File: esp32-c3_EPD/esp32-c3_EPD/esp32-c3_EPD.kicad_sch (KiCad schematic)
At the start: 2 parts, among them U1 ESP32-C3 SuperMini

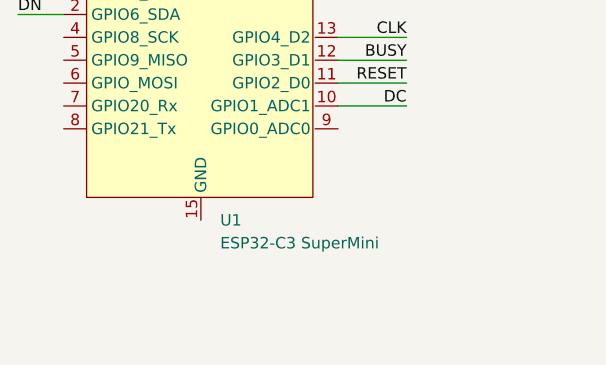
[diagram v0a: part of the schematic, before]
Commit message: ESP32-C3 ePaper
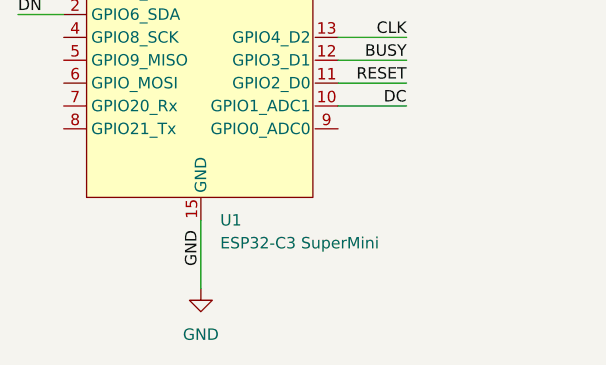
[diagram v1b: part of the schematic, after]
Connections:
- net GND: now also U1.15 (GND)
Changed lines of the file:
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@@
+	(wire
+		(pts
+			(xy 120.65 116.84) (xy 120.65 124.46)
+		)
+		(stroke
+			(width 0)
+			(type default)
+		)
+	)
 	(wire
 		(pts
@@
 	(label "DC"
 		(at 195.58 95.25 90)
+		(effects
+			(font
+				(size 1.27 1.27)
+			)
+			(justify left bottom)
+		)
+	)
+	(label "GND"
+		(at 120.65 121.92 90)
 		(effects
 			(font
@@
 					(unit 1)
 				)
+			)
+		)
+	)
+	(symbol
+		(lib_id "power:GND")
+		(at 120.65 124.46 0)
+		(unit 1)
+		(exclude_from_sim no)
+		(in_bom yes)
+		(on_board yes)
+		(dnp no)
+		(fields_autoplaced yes)
+		(property "Reference" "#PWR01"
+			(at 120.65 130.81 0)
+			(effects
+				(font
+					(size 1.27 1.27)
+				)
+				(hide yes)
+			)
+		)
+		(property "Value" "GND"
+			(at 120.65 129.54 0)
+			(effects
+				(font
+					(size 1.27 1.27)
+				)
+			)
+		)
+		(property "Footprint" ""
+			(at 120.65 124.46 0)
+			(effects
+				(font
+					(size 1.27 1.27)
+				)
+				(hide yes)
+			)
+		)
+		(property "Datasheet" ""
+			(at 120.65 124.46 0)
+			(effects
+				(font
+					(size 1.27 1.27)
+				)
+				(hide yes)
+			)
+		)
+		(property "Description" "Power symbol creates a global label with name \"GND\" , ground"
+			(at 120.65 124.46 0)
+			(effects
+				(font
+					(size 1.27 1.27)
+				)
+				(hide yes)
+			)
+		)
+		(pin "1"
+		)
+		(instances
+			(project ""
+				(path "/344294fb-c5f2-408b-9dcd-2ef32aaa9090"
+					(reference "#PWR01")
+					(unit 1)
+				)

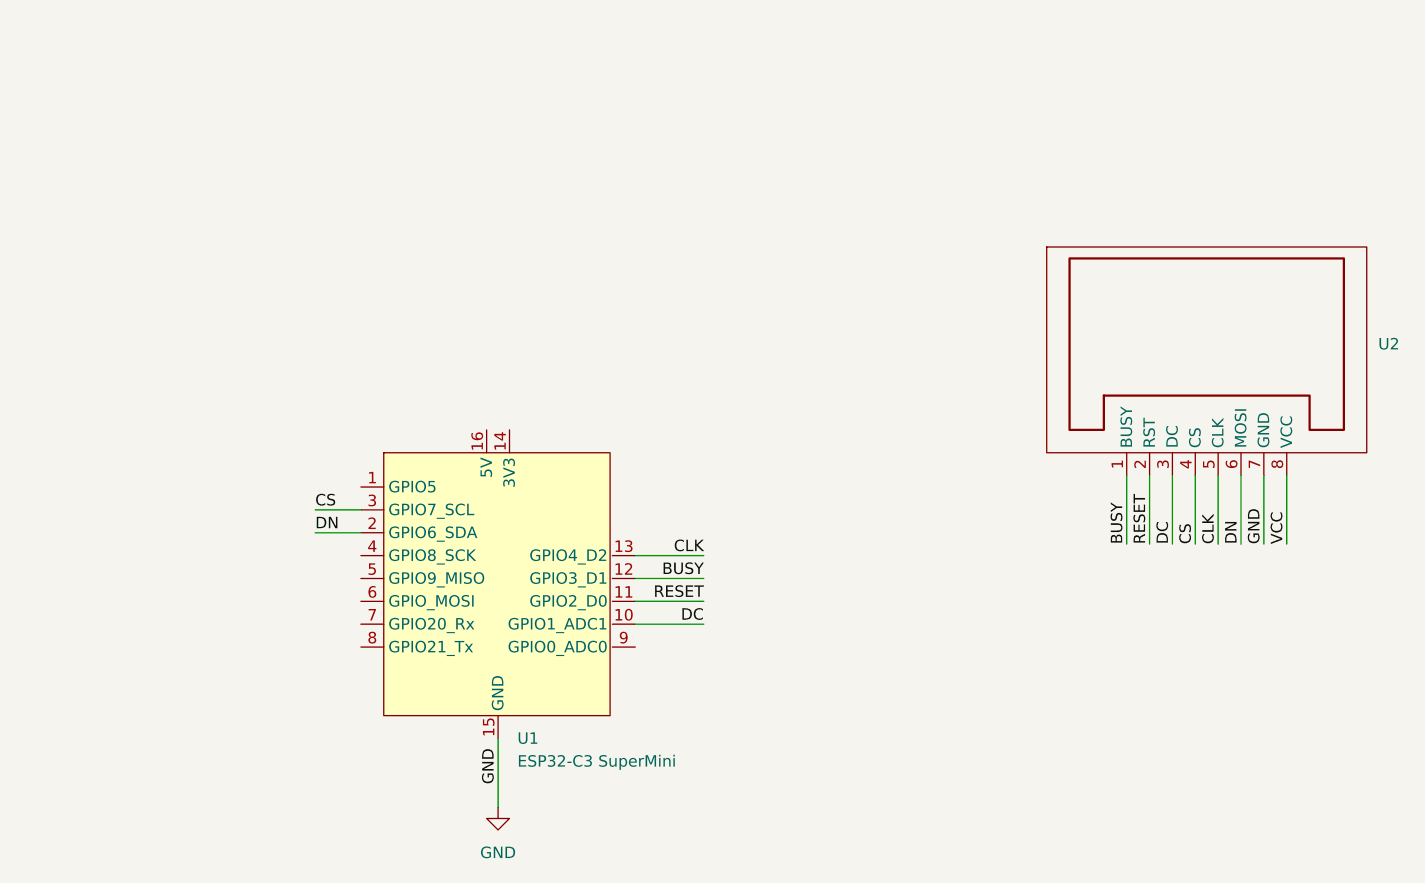
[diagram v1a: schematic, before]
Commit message: ESP32-C3 ePaper
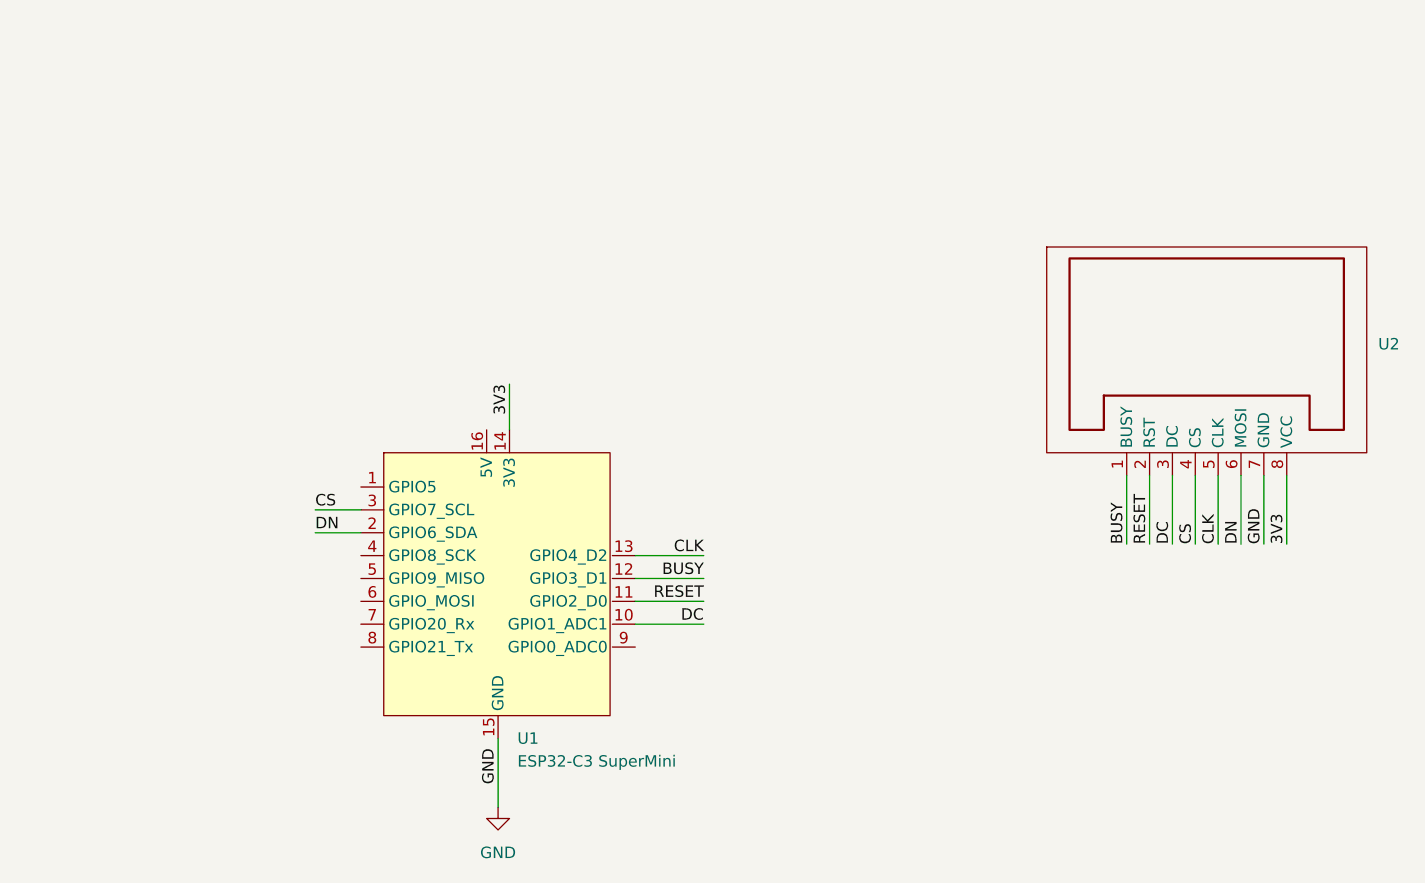
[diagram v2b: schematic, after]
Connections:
- net VCC is gone; now on net 3V3: U2.8 (VCC)
- net 3V3: now reaches U1.14 (3V3)
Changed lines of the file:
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@@
+	(wire
+		(pts
+			(xy 121.92 77.47) (xy 121.92 82.55)
+		)
+		(stroke
+			(width 0)
+			(type default)
+		)
+	)
 	(wire
 		(pts
@@
 		)
 	)
-	(label "VCC"
+	(label "3V3"
+		(at 121.92 77.47 270)
+		(effects
+			(font
+				(size 1.27 1.27)
+			)
+			(justify right bottom)
+		)
+	)
+	(label "3V3"
 		(at 208.28 95.25 90)
 		(effects

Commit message: .
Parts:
- removed U2: ~, symbol Alexander Symbols Library:ePaper
- added J1: e-Paper, Alexander Footprints Library:Conn_ePaper, symbol Alexander Symbols Library:Conn_ePaper_01x08
- U1: footprint Alexander Footprint Library:ESP32-C3_SuperMini -> Alexander Footprints Library:ESP32-C3_SuperMini
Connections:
- net 3V3: now also J1.Vcc
- net BUSY: now also J1.BUSY
- net CLK: now also J1.CLK
- net CS: now also J1.DC
- net DC: now also J1.RST
- net DN: now also J1.DIN
- net GND: now also J1.GND
- net RESET: now also J1.CS
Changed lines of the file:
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@@
 	(wire
 		(pts
-			(xy 198.12 87.63) (xy 198.12 95.25)
+			(xy 144.78 53.34) (xy 158.75 53.34)
 		)
 		(stroke
@@
 	(wire
 		(pts
-			(xy 190.5 87.63) (xy 190.5 95.25)
-		)
-		(stroke
-			(width 0)
-			(type default)
-		)
-	)
-	(wire
-		(pts
-			(xy 208.28 87.63) (xy 208.28 95.25)
+			(xy 144.78 45.72) (xy 158.75 45.72)
+		)
+		(stroke
+			(width 0)
+			(type default)
+		)
+	)
+	(wire
+		(pts
+			(xy 144.78 43.18) (xy 158.75 43.18)
 		)
 		(stroke
@@
 	(wire
 		(pts
-			(xy 193.04 87.63) (xy 193.04 95.25)
-		)
-		(stroke
-			(width 0)
-			(type default)
-		)
-	)
-	(wire
-		(pts
-			(xy 203.2 87.63) (xy 203.2 95.25)
-		)
-		(stroke
-			(width 0)
-			(type default)
-		)
-	)
-	(wire
-		(pts
-			(xy 195.58 87.63) (xy 195.58 95.25)
-		)
-		(stroke
-			(width 0)
-			(type default)
-		)
-	)
-	(wire
-		(pts
-			(xy 200.66 87.63) (xy 200.66 95.25)
-		)
-		(stroke
-			(width 0)
-			(type default)
-		)
-	)
-	(wire
-		(pts
-			(xy 205.74 87.63) (xy 205.74 95.25)
+			(xy 144.78 48.26) (xy 158.75 48.26)
+		)
+		(stroke
+			(width 0)
+			(type default)
+		)
+	)
+	(wire
+		(pts
+			(xy 144.78 58.42) (xy 158.75 58.42)
+		)
+		(stroke
+			(width 0)
+			(type default)
+		)
+	)
+	(wire
+		(pts
+			(xy 144.78 50.8) (xy 158.75 50.8)
+		)
+		(stroke
+			(width 0)
+			(type default)
+		)
+	)
+	(wire
+		(pts
+			(xy 144.78 55.88) (xy 158.75 55.88)
+		)
+		(stroke
+			(width 0)
+			(type default)
+		)
+	)
+	(wire
+		(pts
+			(xy 144.78 60.96) (xy 158.75 60.96)
 		)
 		(stroke
@@
 	)
 	(label "GND"
-		(at 205.74 95.25 90)
+		(at 144.78 60.96 0)
 		(effects
 			(font
@@
 	)
 	(label "3V3"
-		(at 208.28 95.25 90)
+		(at 144.78 43.18 0)
 		(effects
 			(font
@@
 	)
 	(label "RESET"
-		(at 193.04 95.25 90)
+		(at 144.78 48.26 0)
 		(effects
 			(font
@@
 	)
 	(label "DN"
-		(at 203.2 95.25 90)
+		(at 144.78 58.42 0)
 		(effects
 			(font
@@
 	)
 	(label "BUSY"
-		(at 190.5 95.25 90)
+		(at 144.78 45.72 0)
 		(effects
 			(font
@@
 	)
 	(label "CS"
-		(at 198.12 95.25 90)
+		(at 144.78 53.34 0)
 		(effects
 			(font
@@
 	)
 	(label "DC"
-		(at 195.58 95.25 90)
+		(at 144.78 50.8 0)
 		(effects
 			(font
@@
 	)
 	(label "CLK"
-		(at 200.66 95.25 90)
+		(at 144.78 55.88 0)
 		(effects
 			(font
@@
 			)
 		)
-		(property "Footprint" "Alexander Footprint Library:ESP32-C3_SuperMini"
+		(property "Footprint" "Alexander Footprints Library:ESP32-C3_SuperMini"
 			(at 94.234 79.502 0)
 			(effects
@@
 				(path "/344294fb-c5f2-408b-9dcd-2ef32aaa9090"
 					(reference "U1")
-					(unit 1)
-				)
-			)
-		)
-	)
-	(symbol
-		(lib_id "Alexander Symbols Library:ePaper")
-		(at 199.39 59.69 0)
-		(unit 1)
-		(exclude_from_sim no)
-		(in_bom yes)
-		(on_board yes)
-		(dnp no)
-		(fields_autoplaced yes)
-		(property "Reference" "U2"
-			(at 218.44 73.0249 0)
-			(effects
-				(font
-					(size 1.27 1.27)
-				)
-				(justify left)
-			)
-		)
-		(property "Value" "~"
-			(at 218.44 74.93 0)
-			(effects
-				(font
-					(size 1.27 1.27)
-				)
-				(justify left)
-			)
-		)
-		(property "Footprint" ""
-			(at 199.39 59.69 0)
-			(effects
-				(font
-					(size 1.27 1.27)
-				)
-				(hide yes)
-			)
-		)
-		(property "Datasheet" ""
-			(at 199.39 59.69 0)
-			(effects
-				(font
-					(size 1.27 1.27)
-				)
-				(hide yes)
-			)
-		)
-		(property "Description" ""
-			(at 199.39 59.69 0)
-			(effects
-				(font
-					(size 1.27 1.27)
-				)
-				(hide yes)
-			)
-		)
-		(pin "1"
-		)
-		(pin "4"
-		)
-		(pin "3"
-		)
-		(pin "5"
-		)
-		(pin "7"
-		)
-		(pin "6"
-		)
-		(pin "8"
-		)
-		(pin "2"
-		)
-		(instances
-			(project ""
-				(path "/344294fb-c5f2-408b-9dcd-2ef32aaa9090"
-					(reference "U2")
 					(unit 1)
 				)
@@
 					(unit 1)
 				)
+			)
+		)
+	)
+	(symbol
+		(lib_id "Alexander Symbols Library:Conn_ePaper_01x08")
+		(at 163.83 50.8 0)
+		(mirror y)
+		(unit 1)
+		(exclude_from_sim no)
+		(in_bom yes)
+		(on_board yes)
+		(dnp no)
+		(property "Reference" "J1"
+			(at 163.195 38.1 0)
+			(effects
+				(font
+					(size 1.27 1.27)
+				)
+			)
+		)
+		(property "Value" "e-Paper"
+			(at 163.195 40.64 0)
+			(effects
+				(font
+					(size 1.27 1.27)
+				)
+			)
+		)
+		(property "Footprint" "Alexander Footprints Library:Conn_ePaper"
+			(at 163.83 55.88 0)
+			(effects
+				(font
+					(size 1.27 1.27)
+				)
+				(hide yes)
+			)
+		)
+		(property "Datasheet" "~"
+			(at 165.1 52.07 0)
+			(effects
+				(font
+					(size 1.27 1.27)
+				)
+				(hide yes)
+			)
+		)
+		(property "Description" "Generic connector, single row, 01x08, script generated"
+			(at 163.83 50.8 0)
+			(effects
+				(font
+					(size 1.27 1.27)
+				)
+				(hide yes)
+			)
+		)
+		(pin "GND"
+		)
+		(pin "RST"
+		)
+		(pin "CLK"
+		)
+		(pin "CS"
+		)
+		(pin "DC"
+		)
+		(pin "BUSY"
+		)
+		(pin "Vcc"
+		)
+		(pin "DIN"
+		)
+		(instances
+			(project ""
+				(path "/344294fb-c5f2-408b-9dcd-2ef32aaa9090"
+					(reference "J1")
+					(unit 1)
+				)

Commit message: .
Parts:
- added U2: ESP32-C3 WROOM, symbol Alexander Symbols Library 1:ESP32-C3_Mini
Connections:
- net 3V3: now also U2.1 (3V3)
- net BUSY: now also U2.15 (GPIO3)
- net CLK: now also U2.3 (GPIO4)
- net CS: now also U2.6 (GPIO7)
- net DN: now also U2.5 (GPIO6)
- net GND: now also U2.9 (GND)
- net RESET: now also U2.16 (GPIO2)
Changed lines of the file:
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@@
+	(wire
+		(pts
+			(xy 67.31 57.15) (xy 73.66 57.15)
+		)
+		(stroke
+			(width 0)
+			(type default)
+		)
+	)
+	(wire
+		(pts
+			(xy 105.41 54.61) (xy 113.03 54.61)
+		)
+		(stroke
+			(width 0)
+			(type default)
+		)
+	)
+	(wire
+		(pts
+			(xy 67.31 59.69) (xy 73.66 59.69)
+		)
+		(stroke
+			(width 0)
+			(type default)
+		)
+	)
+	(wire
+		(pts
+			(xy 67.31 52.07) (xy 73.66 52.07)
+		)
+		(stroke
+			(width 0)
+			(type default)
+		)
+	)
 	(wire
 		(pts
@@
 	(wire
 		(pts
+			(xy 67.31 46.99) (xy 73.66 46.99)
+		)
+		(stroke
+			(width 0)
+			(type default)
+		)
+	)
+	(wire
+		(pts
 			(xy 135.89 99.06) (xy 143.51 99.06)
 		)
@@
 	(wire
 		(pts
+			(xy 105.41 52.07) (xy 113.03 52.07)
+		)
+		(stroke
+			(width 0)
+			(type default)
+		)
+	)
+	(wire
+		(pts
 			(xy 121.92 77.47) (xy 121.92 82.55)
+		)
+		(stroke
+			(width 0)
+			(type default)
+		)
+	)
+	(wire
+		(pts
+			(xy 67.31 67.31) (xy 73.66 67.31)
 		)
 		(stroke
@@
 	)
 	(label "3V3"
+		(at 67.31 46.99 0)
+		(effects
+			(font
+				(size 1.27 1.27)
+			)
+			(justify left bottom)
+		)
+	)
+	(label "DN"
+		(at 67.31 57.15 0)
+		(effects
+			(font
+				(size 1.27 1.27)
+			)
+			(justify left bottom)
+		)
+	)
+	(label "3V3"
 		(at 121.92 77.47 270)
 		(effects
@@
 		)
 	)
+	(label "CLK"
+		(at 67.31 52.07 0)
+		(effects
+			(font
+				(size 1.27 1.27)
+			)
+			(justify left bottom)
+		)
+	)
 	(label "CS"
 		(at 100.33 91.44 0)
@@
 		)
 	)
+	(label "CS"
+		(at 67.31 59.69 0)
+		(effects
+			(font
+				(size 1.27 1.27)
+			)
+			(justify left bottom)
+		)
+	)
+	(label "RESET"
+		(at 113.03 52.07 180)
+		(effects
+			(font
+				(size 1.27 1.27)
+			)
+			(justify right bottom)
+		)
+	)
 	(label "DC"
 		(at 143.51 104.14 180)
@@
 		)
 	)
+	(label "BUSY"
+		(at 113.03 54.61 180)
+		(effects
+			(font
+				(size 1.27 1.27)
+			)
+			(justify right bottom)
+		)
+	)
 	(label "DN"
 		(at 144.78 58.42 0)
@@
 	(label "GND"
 		(at 120.65 121.92 90)
+		(effects
+			(font
+				(size 1.27 1.27)
+			)
+			(justify left bottom)
+		)
+	)
+	(label "GND"
+		(at 67.31 67.31 0)
 		(effects
 			(font
@@
 					(unit 1)
 				)
+			)
+		)
+	)
+	(symbol
+		(lib_id "Alexander Symbols Library 1:ESP32-C3_Mini")
+		(at 88.9 41.91 0)
+		(unit 1)
+		(exclude_from_sim no)
+		(in_bom yes)
+		(on_board yes)
+		(dnp no)
+		(fields_autoplaced yes)
+		(property "Reference" "U2"
+			(at 89.535 39.37 0)
+			(effects
+				(font
+					(size 1.27 1.27)
+				)
+			)
+		)
+		(property "Value" "ESP32-C3 WROOM"
+			(at 89.535 41.91 0)
+			(effects
+				(font
+					(size 1.27 1.27)
+				)
+			)
+		)
+		(property "Footprint" ""
+			(at 88.9 41.91 0)
+			(effects
+				(font
+					(size 1.27 1.27)
+				)
+				(hide yes)
+			)
+		)
+		(property "Datasheet" ""
+			(at 88.9 41.91 0)
+			(effects
+				(font
+					(size 1.27 1.27)
+				)
+				(hide yes)
+			)
+		)
+		(property "Description" "ESP32-C3 WROOM BRD"
+			(at 89.408 40.386 0)
+			(effects
+				(font
+					(size 1.27 1.27)
+				)
+				(hide yes)
+			)
+		)
+		(pin "1"
+		)
+		(pin "2"
+		)
+		(pin "3"
+		)
+		(pin "4"
+		)
+		(pin "5"
+		)
+		(pin "6"
+		)
+		(pin "16"
+		)
+		(pin "12"
+		)
+		(pin "11"
+		)
+		(pin "17"
+		)
+		(pin "7"
+		)
+		(pin "8"
+		)
+		(pin "13"
+		)
+		(pin "15"
+		)
+		(pin "10"
+		)
+		(pin "14"
+		)
+		(pin "9"
+		)
+		(pin "18"
+		)
+		(instances
+			(project ""
+				(path "/344294fb-c5f2-408b-9dcd-2ef32aaa9090"
+					(reference "U2")
+					(unit 1)
+				)
